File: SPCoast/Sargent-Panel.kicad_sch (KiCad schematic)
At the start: 9 parts, among them U1 0x2C

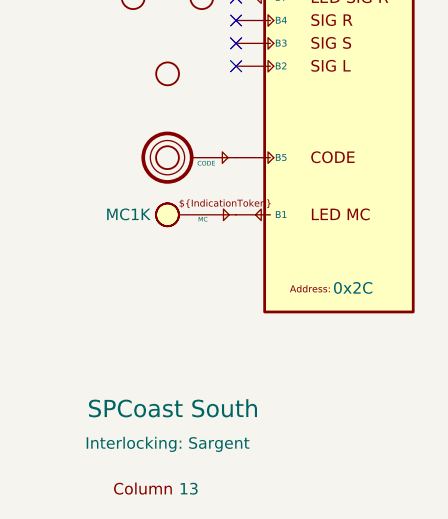
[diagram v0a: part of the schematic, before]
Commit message: chore(kicad): owner mockup: explicit seam wiring on Luchessa and South-cTc, host and bus pins
Owner's edits, committed as they stand (2026-10-21), before scripted edits build on them.

- Interlocking gains Codeline and Host pins; MAIN HOUSE's Interlocking pin is Codeline.
- OfficeUnit gains Host and Codeline pins; JohnCTC desk processor drawn on South-cTc.
- Processor gains Transport and IO pins; MAX7313 and MCP23017 gain an I2C bus pin.
- Transports: Codeline pin renamed Host; JMRI_MQTT instance added; Loconet removed.
- Encodings' pin renamed Transport; Luchessa's 506 and Bit Packing instances removed.
- SPCoastApp virtual host (FieldUnit_Virtual) hosts CMRInet and JMRI_MQTT.
- Luchessa: unit, houses and Time Coded on one net; Host to its own processor;
  panel MAX7313s on the desk bus (OfficeBus).
- Watsonville, Caltrain, Interchange: first-pass Processor placeholders, to be redrawn.

Verified: netlist and ERC exported from the saved project; field diff against the
committed netlist shows no per-instance field lost.
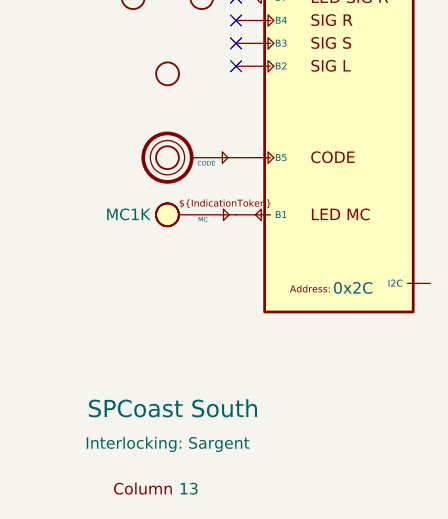
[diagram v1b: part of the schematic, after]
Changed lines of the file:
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@@
 		(pin "16"
+		)
+		(pin "17"
 		)
 		(instances
